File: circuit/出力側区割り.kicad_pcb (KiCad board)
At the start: 2 copper layers, 95 x 54.5 mm, 47 parts, among them IC1 TLP521, IC2 TLP521, IC3 TLP521, IC4 TLP521, IC5 TLP521, IC6 TLP521, J1 RJ45_8pin, J2 RJ45_8pin, J3 servo0, J4 servo1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

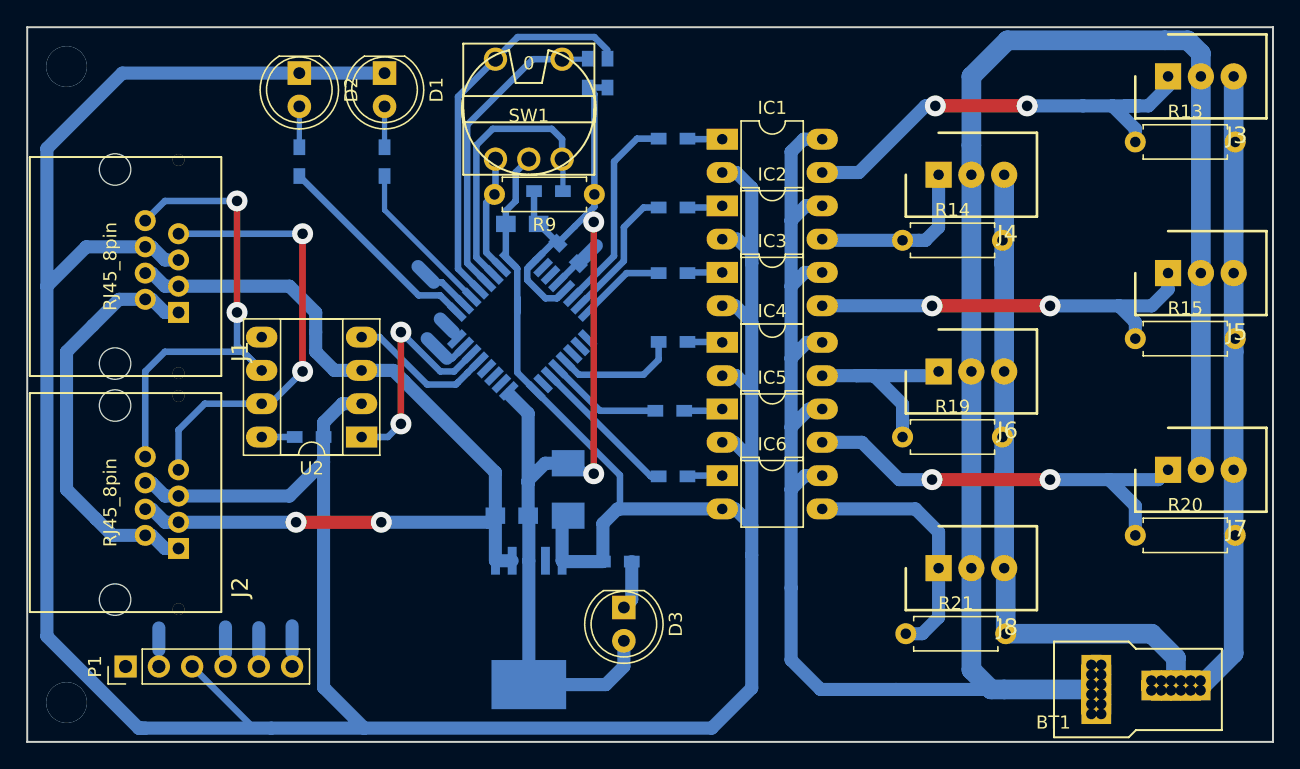
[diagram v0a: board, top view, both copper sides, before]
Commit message: 基板加工用にデータを変更したやつを追加
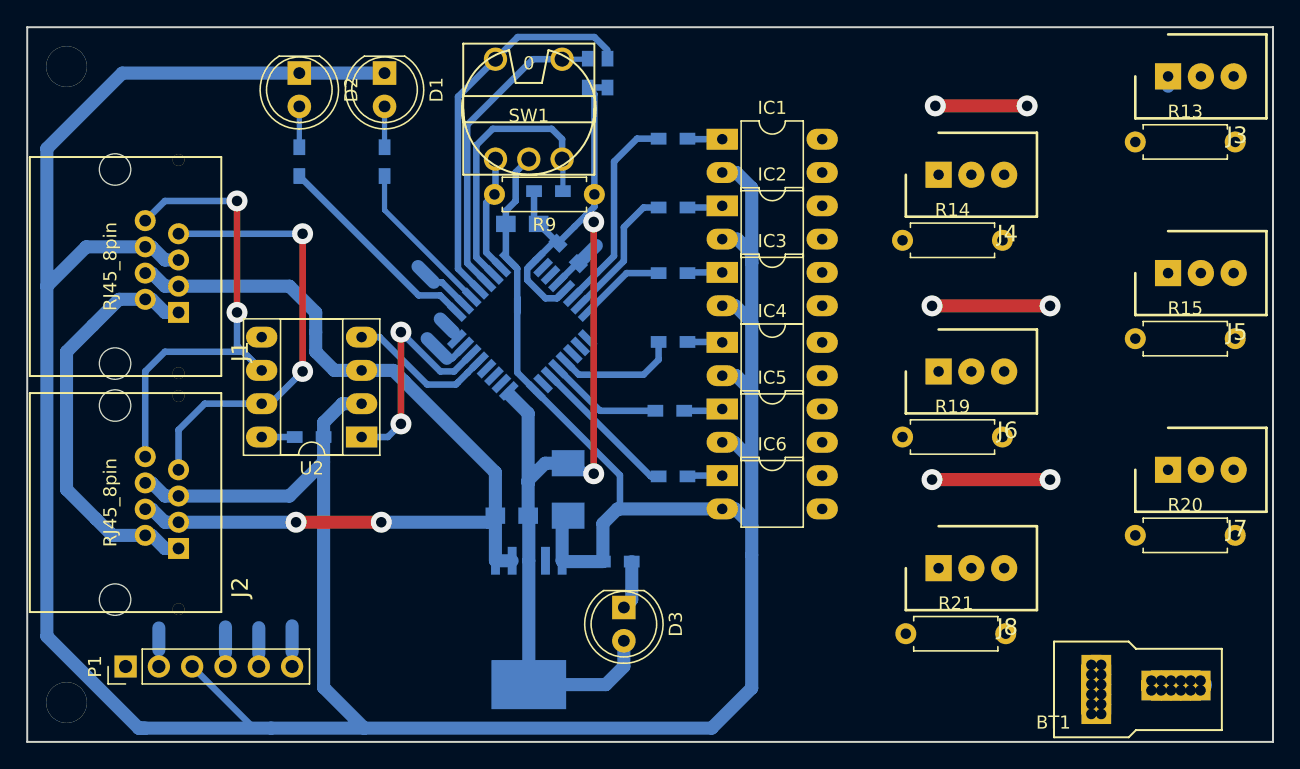
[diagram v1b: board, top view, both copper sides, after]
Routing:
- net +7.4V: track 179.2 -> 0.00 mm
- net GNDPWR: track 107.4 -> 2.52 mm
- net Net-(IC3-Pad3): track 31.2 -> 0.00 mm, vias 2 -> 0
- net Net-(IC1-Pad3): track 34.3 -> 7.75 mm
- net Net-(IC5-Pad3): track 32.9 -> 9.00 mm
- net Net-(IC6-Pad3): track 19.1 -> 0.00 mm
- net Net-(IC4-Pad3): track 15.9 -> 0.46 mm
- net Net-(IC2-Pad3): track 13.5 -> 0.25 mm
- net (no net): track 0.00 -> 9.01 mm, vias 2 -> 4

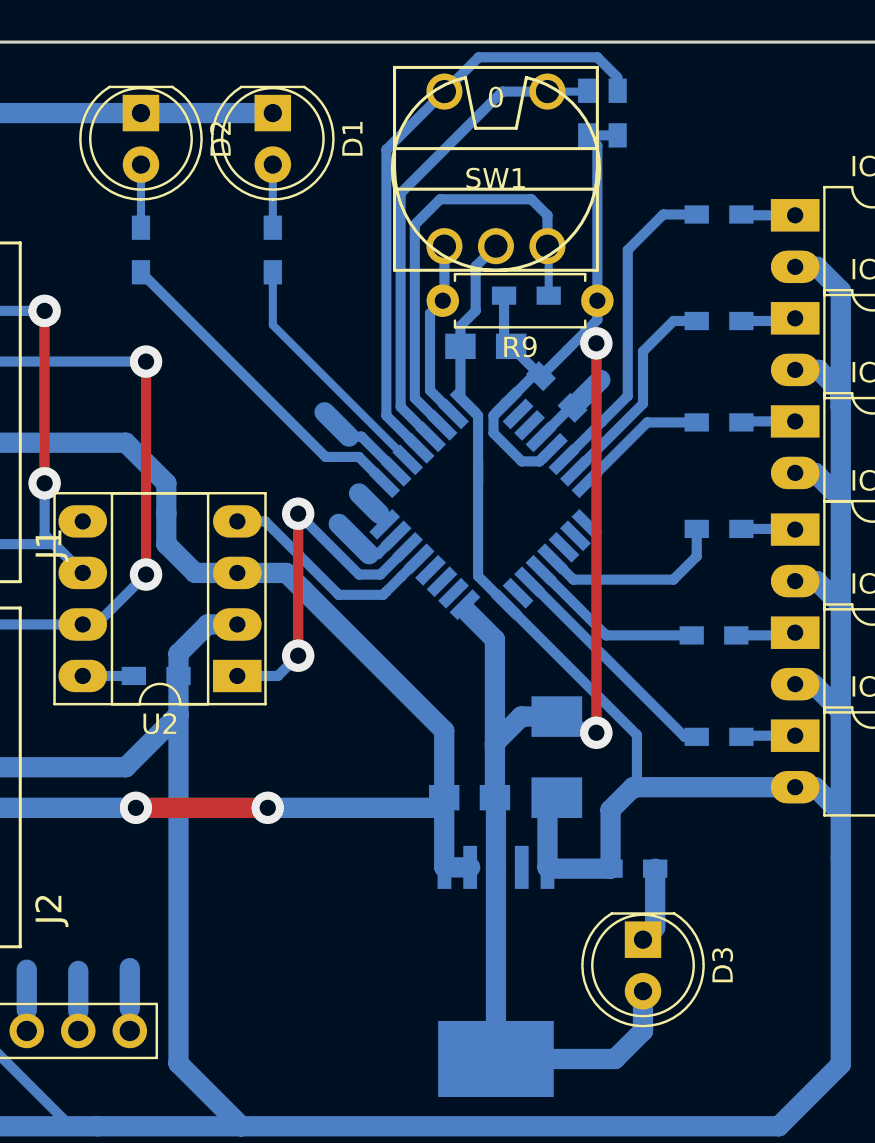
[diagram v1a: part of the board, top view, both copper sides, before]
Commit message: チップ抵抗の大きさ変更とガーバー出力のための手直し
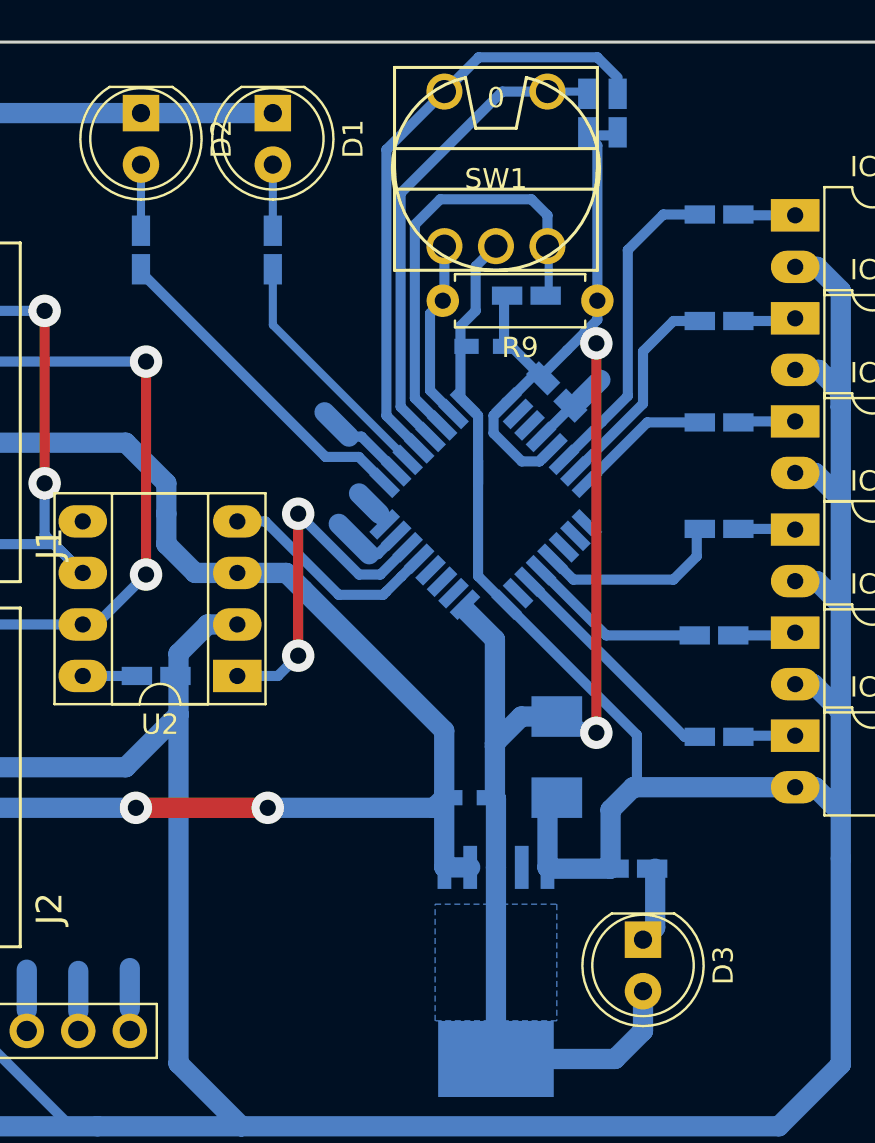
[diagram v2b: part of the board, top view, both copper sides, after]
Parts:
- C1, C2: footprint Capacitors_SMD:C_0805_HandSoldering -> Capacitors_SMD:C_0603_HandSoldering
- R1, R10, R11, R12, R16, R17, R18, R2, R3, R4, R5, R6, R7, R8: footprint Resistors_SMD:R_0603_HandSoldering -> YASU:R_0603_HandSoldering_LP
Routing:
- net (no net): track 9.01 -> 25.0 mm, vias 4 -> 8
- net Net-(IC5-Pad3): track 9.00 -> 0.00 mm, vias 2 -> 0
- net Net-(IC1-Pad3): track 7.75 -> 0.75 mm, vias 2 -> 0
- added copper zone on B.Cu, net +3V3
